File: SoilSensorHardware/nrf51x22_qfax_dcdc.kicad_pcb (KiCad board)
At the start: 2 copper layers, 25 x 100 mm, 116 parts, among them J1 Conn_02x07_Odd_Even, J2 Conn_01x06, U1 nrf52810-QFAA-T, U2 TLC555xD, X1 Crystal-4, X2 32.768kHz

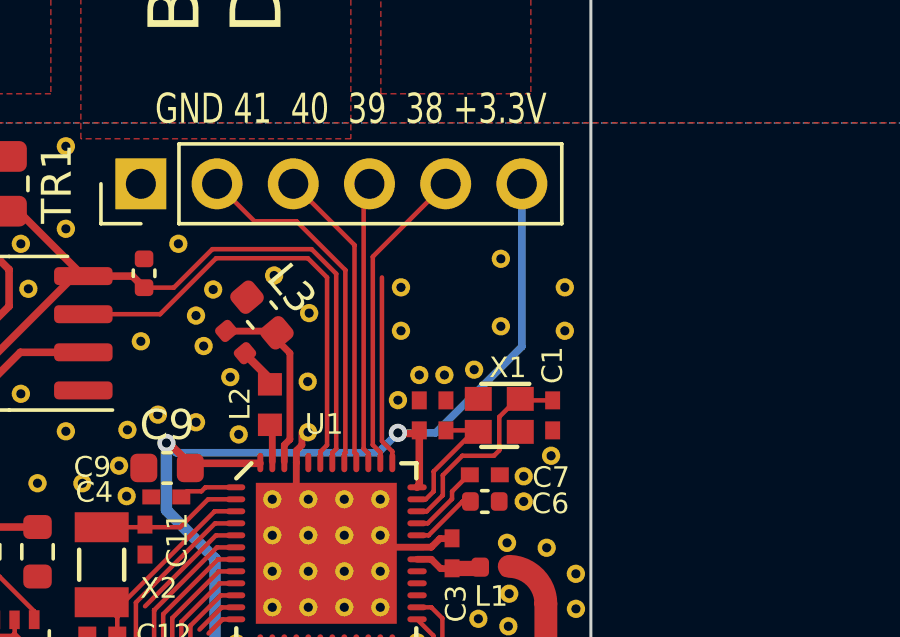
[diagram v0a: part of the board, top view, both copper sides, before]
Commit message: Moved power trace from under HF crystal
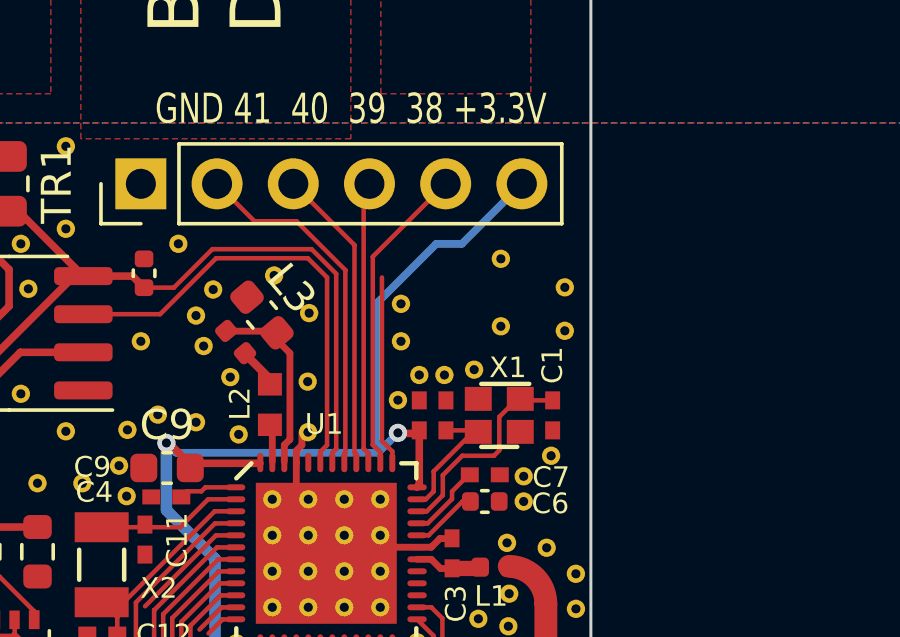
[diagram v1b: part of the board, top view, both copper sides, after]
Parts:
- moved REF** 0.55 mm to (136.7, 139.0)
- moved REF** 0.35 mm to (136.7, 140.2)
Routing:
- net +3.3v: track 49.4 -> 50.1 mm
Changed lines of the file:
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@@
   )
   (footprint "dcdc:VIA-0.6096" (layer "F.Cu")
-    (at 136.6706 138.45178)
+    (at 136.6706 139)
     (attr through_hole)
     (fp_text reference "REF**" (at 0 2.54) (layer "F.SilkS") hide
@@
   )
   (footprint "dcdc:VIA-0.6096" (layer "F.Cu")
-    (at 136.6706 139.89958)
+    (at 136.6706 140.25)
     (attr through_hole)
     (fp_text reference "REF**" (at 0 2.54) (layer "F.SilkS") hide
@@
   (via (at 128.85139 143.63938) (size 0.6096) (drill 0.3048) (layers "F.Cu" "B.Cu") (net 14))
   (segment (start 129.17558 143.96358) (end 135.9086 143.96358) (width 0.254) (layer "B.Cu") (net 14))
-  (segment (start 137.82359 143.30318) (end 140.7 140.42677) (width 0.254) (layer "B.Cu") (net 14))
   (segment (start 130.47428 150.89907) (end 130.47428 147.50018) (width 0.381) (layer "B.Cu") (net 14))
   (segment (start 129.28177 152.09158) (end 123.0308 152.09158) (width 0.381) (layer "B.Cu") (net 14))
   (segment (start 135.9086 143.96358) (end 136.569 143.30318) (width 0.254) (layer "B.Cu") (net 14))
   (segment (start 128.85139 143.63938) (end 129.17558 143.96358) (width 0.254) (layer "B.Cu") (net 14))
-  (segment (start 140.7 140.42677) (end 140.7 135) (width 0.254) (layer "B.Cu") (net 14))
+  (segment (start 135.9086 143.96358) (end 135.9086 138.93921) (width 0.254) (layer "B.Cu") (net 14))
   (segment (start 131.8068 152.08158) (end 132.33158 152.08158) (width 0.35) (layer "B.Cu") (net 14))
+  (segment (start 138.7 137) (end 140.7 135) (width 0.254) (layer "B.Cu") (net 14))
   (segment (start 131.7968 152.09158) (end 131.8068 152.08158) (width 0.381) (layer "B.Cu") (net 14))
   (segment (start 129.28177 152.09158) (end 131.2968 152.09158) (width 0.381) (layer "B.Cu") (net 14))
@@
   (segment (start 132.77 152.52) (end 132.77 153) (width 0.35) (layer "B.Cu") (net 14))
   (segment (start 128.85139 145.87729) (end 128.85139 143.63938) (width 0.381) (layer "B.Cu") (net 14))
+  (segment (start 135.9086 138.93921) (end 137.84781 137) (width 0.254) (layer "B.Cu") (net 14))
+  (segment (start 137.84781 137) (end 138.7 137) (width 0.254) (layer "B.Cu") (net 14))
   (segment (start 132.33158 152.08158) (end 132.77 152.52) (width 0.35) (layer "B.Cu") (net 14))
   (segment (start 128.85139 145.87729) (end 130.47428 147.50018) (width 0.381) (layer "B.Cu") (net 14))
-  (segment (start 136.569 143.30318) (end 137.82359 143.30318) (width 0.254) (layer "B.Cu") (net 14))
   (segment (start 129.966285 151.407065) (end 129.28177 152.09158) (width 0.381) (layer "B.Cu") (net 14))
   (segment (start 131.2968 152.09158) (end 131.7968 152.09158) (width 0.381) (layer "B.Cu") (net 14))
